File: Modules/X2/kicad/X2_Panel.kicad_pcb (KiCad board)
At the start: 2 copper layers, 9.8 x 128.5 mm, 12 parts

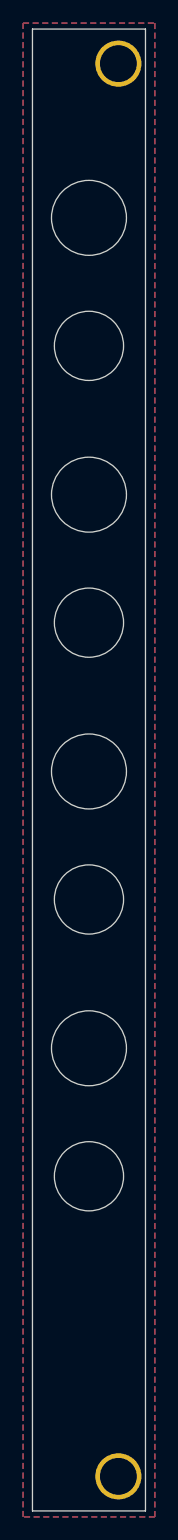
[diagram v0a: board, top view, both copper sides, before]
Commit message: Add Interactive BOMs, resave all PCBs, move VU to THT.
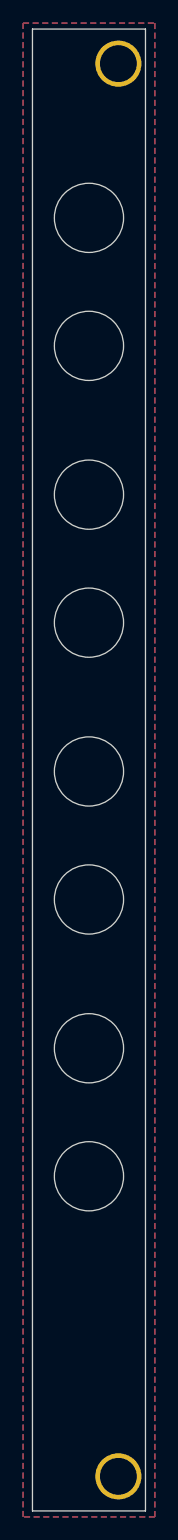
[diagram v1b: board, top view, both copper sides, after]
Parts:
- removed the REF** at (88.9, 41.0)
- removed the REF** at (88.9, 113.0)
- removed the REF** at (88.9, 65.0)
- removed the REF** at (88.9, 89.0)
- added REF**: Panel Jack, Panels:Panel Jack, F.Cu at (88.9, 113.0)
- added REF**: Panel Jack, Panels:Panel Jack, F.Cu at (88.9, 41.0)
- added REF**: Panel Jack, Panels:Panel Jack, F.Cu at (88.9, 89.0)
- added REF**: Panel Jack, Panels:Panel Jack, F.Cu at (88.9, 65.0)

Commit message: Update X2 to new version.
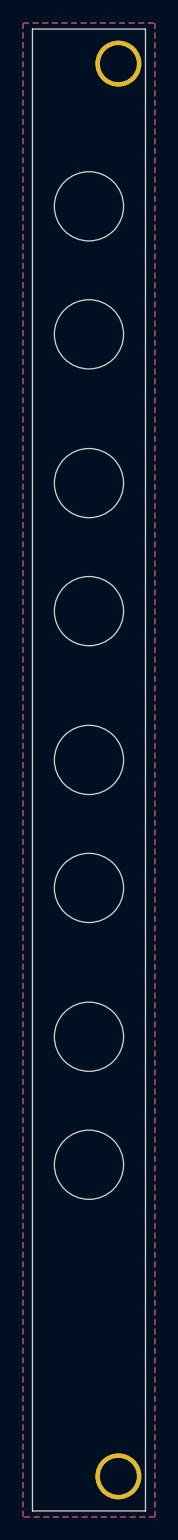
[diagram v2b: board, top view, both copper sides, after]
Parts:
- moved G*** 1.00 mm to (88.8, 87.8)
- moved REF** 1.00 mm to (88.9, 75.1)
- moved REF** 1.00 mm to (88.9, 99.1)
- moved REF** 1.00 mm to (88.9, 112.0)
- moved REF** 1.00 mm to (88.9, 40.0)
- moved REF** 1.00 mm to (88.9, 88.0)
- moved REF** 1.00 mm to (88.9, 51.1)
- moved REF** 1.00 mm to (88.9, 64.0)
- moved REF** 1.00 mm to (88.9, 123.1)
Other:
- board text added: "X2 v1.1"
- board text removed: "JLCJLCJLCJLC"
- board text removed: "X2 v1.0"
